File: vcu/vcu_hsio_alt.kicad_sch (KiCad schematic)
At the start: 51 parts, among them J5 FSUK_RTD, Q2 FDN359BN, Q3 FDN359BN, Q4 FDN359BN, Q5 FDN359BN, Q6 FDN359BN, Q7 FDN359BN, Q8 FDN359BN, U10 4504, U11 4504, U12 4504

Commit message: unbreaking git hopefully
pls work pls work pls work pls work pls work pls work pls work pls work pls work pls work pls work pls work pls work pls work pls work pls work pls work pls work pls work pls work pls work pls work pls work pls work
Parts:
- removed #SP1: KP1600, symbol Device:Speaker
- removed C49, C52: 1uF, Capacitor_SMD:C_0402_1005Metric, symbol Device:C_Small
- removed C50, C51: 0.1uF, Capacitor_SMD:C_0402_1005Metric, symbol Device:C_Small
- removed D14, D15, D16, D17, D18, D19, D20, D21: LED, LED_SMD:LED_0402_1005Metric, symbol Device:LED
- removed J5: FSUK_RTD, Connector_PinHeader_2.54mm:PinHeader_1x02_P2.54mm_Vertical, symbol Connector_Generic:Conn_02x01
- removed Q2, Q3, Q4, Q5, Q6, Q7, Q8: FDN359BN, Package_TO_SOT_SMD:SOT-23_Handsoldering, symbol SUFST:FDN359BN
- removed R62, R63, R64, R65, R66, R67, R68, R69: 1.5K, Resistor_SMD:R_0402_1005Metric, symbol Device:R_Small
- removed R70, R71, R72: 8.6K, Resistor_SMD:R_0402_1005Metric, symbol Device:R_Small
- removed R73, R74, R81, R82, R83, R84: 0, Resistor_SMD:R_0402_1005Metric, symbol Device:R_Small
- removed R75: 4.7K, Resistor_SMD:R_0402_1005Metric, symbol Device:R_Small
- removed R76: 1k, Resistor_SMD:R_0402_1005Metric, symbol Device:R_Small
- removed R77: 3k3, Resistor_SMD:R_0402_1005Metric, symbol Device:R_Small
- removed R78, R79, R80, R85, R86, R87: 1K, Resistor_SMD:R_0402_1005Metric, symbol Device:R_Small
- removed U10, U11, U12: 4504, Package_SO:SOIC-16W_5.3x10.2mm_P1.27mm, symbol 4xxx:4504
- removed U9: ~, Package_DFN_QFN:TQFN-32-1EP_5x5mm_P0.5mm_EP3.1x3.1mm_ThermalVias, symbol SUFST:MAX22195
- added #SP2: KP1600, symbol Device:Speaker
- added C64, C67: 1uF, Capacitor_SMD:C_0402_1005Metric, symbol Device:C_Small
- added C65, C66: 0.1uF, Capacitor_SMD:C_0402_1005Metric, symbol Device:C_Small
- added D22, D23, D24, D25, D26, D27, D28, D4: LED, LED_SMD:LED_0402_1005Metric, symbol Device:LED
- added J1: FSUK_RTD, Connector_PinHeader_2.54mm:PinHeader_1x02_P2.54mm_Vertical, symbol Connector_Generic:Conn_02x01
- added Q11, Q12, Q13, Q14, Q15, Q16, Q9: FDN359BN, Package_TO_SOT_SMD:SOT-23_Handsoldering, symbol SUFST:FDN359BN
- added R100, R101, R102, R103, R96, R97, R98, R99: 1.5K, Resistor_SMD:R_0402_1005Metric, symbol Device:R_Small
- added R104, R105, R106: 8.6K, Resistor_SMD:R_0402_1005Metric, symbol Device:R_Small
- added R107, R108, R115, R116, R117, R118: 0, Resistor_SMD:R_0402_1005Metric, symbol Device:R_Small
- added R109: 4.7K, Resistor_SMD:R_0402_1005Metric, symbol Device:R_Small
- added R110: 1k, Resistor_SMD:R_0402_1005Metric, symbol Device:R_Small
- added R111: 3k3, Resistor_SMD:R_0402_1005Metric, symbol Device:R_Small
- added R112, R113, R114, R119, R120, R121: 1K, Resistor_SMD:R_0402_1005Metric, symbol Device:R_Small
- added U15, U16, U22: 4504, Package_SO:SOIC-16W_5.3x10.2mm_P1.27mm, symbol 4xxx:4504
- added U6: ~, Package_DFN_QFN:TQFN-32-1EP_5x5mm_P0.5mm_EP3.1x3.1mm_ThermalVias, symbol SUFST:MAX22195
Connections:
- net +3V3: now also C66.2, C67.2, U15.16 (VDD), U16.1 (VCC), U22.1 (VCC), U6.28 (RDYEN), U6.31 (VDD3)
- net +5V: now also R108.2, R115.2, R116.2
- net +GLV_PROT: now also C64.2, C65.2, R104.1, R107.2, R117.2, R118.2, U6.30 (VDD24)
- net GND: now also C64.1, C65.1, C66.1, C67.1, D22.1 (K), D23.1 (K), D24.1 (K), D25.1 (K), D26.1 (K), D27.1 (K), D28.1 (K), D4.1 (K), Q11.2 (S), Q12.2 (S), Q13.2 (S), Q14.2 (S), Q15.2 (S), Q16.2 (S), Q9.2 (S), R105.2, R106.2, R109.1, R111.1, U15.8 (VSS), U16.8 (VSS), U22.8 (VSS), U6.25 (GND), U6.32 (GND), U6.EX (GND)
- net HSDI_GP1: now also R100.2
- net HSDI_GP10: now also U15.14 (Fin)
- net HSDI_GP2: now also R101.2
- net HSDI_GP3: now also R102.2
- net HSDI_GP4: now also R103.2
- net HSDI_GP5: now also U15.3 (Ain)
- net HSDI_GP6: now also U15.5 (Bin)
- net HSDI_GP7: now also U15.7 (Cin)
- net HSDI_GP8: now also U15.9 (Din)
- net HSDI_GP9: now also U15.11 (Ein)
- net HSDI_SCS1: now also R96.2
- net HSDI_SCS2: now also R97.2
- net HSDI_SCS3: now also R98.2
- net HSDI_SCS4: now also R99.2
- net HSDO_GP1: now also U16.12 (Eout)
- net HSDO_GP2: now also U16.15 (Fout)
- net HSDO_GP3: now also U22.2 (Aout)
- net HSDO_GP4: now also U22.4 (Bout)
- net HSDO_GP6: now also U22.6 (Cout)
- net HSDO_GP7: now also U22.10 (Dout)
- net HSDO_PWM1: now also U22.12 (Eout)
- net HSDO_PWM2: now also U22.15 (Fout)
- net HSDO_SCS1: now also U16.2 (Aout)
- net HSDO_SCS2: now also U16.4 (Bout)
- net HSDO_SCS3: now also U16.6 (Cout)
- net HSDO_SCS4: now also U16.10 (Dout)
- net LATCH_1: now also Q11.1 (G)
- net LATCH_2: now also Q12.1 (G)
- net LED_1: now also R112.2
- net LED_2: now also R113.2
- net LED_3: now also R114.2
- net LED_4: now also R119.2
- net LED_5: now also R120.2
- net LED_6: now also R121.2
- net LEVEL1_RDY: now also R109.2, U6.29 (READY)
- net LSDI_GP1: now also U6.13 (OP5)
- net LSDI_GP2: now also U6.14 (OP6)
- net LSDI_GP3: now also U6.15 (OP7), U6.16 (OP8)
- net LSDI_SCS1: now also U6.9 (OP1)
- net LSDI_SCS10: now also U15.15 (Fout)
- net LSDI_SCS2: now also U6.10 (OP2)
- net LSDI_SCS3: now also U6.11 (OP3)
- net LSDI_SCS4: now also U6.12 (OP4)
- net LSDI_SCS5: now also U15.2 (Aout)
- net LSDI_SCS6: now also U15.4 (Bout)
- net LSDI_SCS7: now also U15.6 (Cout)
- net LSDI_SCS8: now also U15.10 (Dout)
- net LSDI_SCS9: now also U15.12 (Eout)
- net LSDO_GP1: now also U16.11 (Ein)
- net LSDO_GP2: now also U16.14 (Fin)
- net LSDO_GP3: now also U22.3 (Ain)
- net LSDO_GP4: now also U22.5 (Bin)
- net LSDO_GP5: now also U22.7 (Cin)
- net LSDO_GP6: now also U22.9 (Din)
- net LSDO_PWM1: now also U22.11 (Ein)
- net LSDO_PWM2: now also U22.14 (Fin)
- net LSDO_SCS1: now also U16.3 (Ain)
- net LSDO_SCS2: now also U16.5 (Bin)
- net LSDO_SCS3: now also U16.7 (Cin)
- net LSDO_SCS4: now also U16.9 (Din)
- net LSD_LED_3: now also Q13.1 (G)
- net LSD_LED_4: now also Q14.1 (G)
- net LSD_LED_5: now also Q15.1 (G)
- net LSD_LED_6: now also Q16.1 (G)
- net LSD_R2D: now also Q9.1 (G), R111.2
- net R2DS-: now also J1.2 (Pin_2), R110.2
- new net: Q13.3 (D), R114.1
- new net: Q14.3 (D), R119.1
- new net: R107.1, R108.1, U15.1 (VCC)
- new net: Q15.3 (D), R120.1
- new net: J1.1 (Pin_1), Q9.3 (D), R110.1
- new net: R97.1, U6.3 (IN2)
- new net: R96.1, U6.1 (IN1)
- new net: D25.2 (A), U6.17 (LED5)
- new net: R100.1, U6.18 (IN5)
- new net: D26.2 (A), U6.19 (LED6)
- new net: D4.2 (A), U6.2 (LED1)
- new net: R101.1, U6.20 (IN6)
- new net: D27.2 (A), U6.21 (LED7)
- new net: R102.1, U6.22 (IN7)
- new net: D28.2 (A), U6.23 (LED8)
- new net: R103.1, U6.24 (IN8)
- new net: R106.1, U6.26 (REFDI)
- new net: R104.2, R105.1, U6.27 (EXTVM)
- new net: D22.2 (A), U6.4 (LED2)
- new net: R98.1, U6.5 (IN3)
- new net: D23.2 (A), U6.6 (LED3)
- new net: R99.1, U6.7 (IN4)
- new net: D24.2 (A), U6.8 (LED4)
- new net: R116.1, R118.1, U22.16 (VDD)
- new net: Q11.3 (D), R112.1
- new net: Q12.3 (D), R113.1
- new net: Q16.3 (D), R121.1
- new net: R115.1, R117.1, U16.16 (VDD)

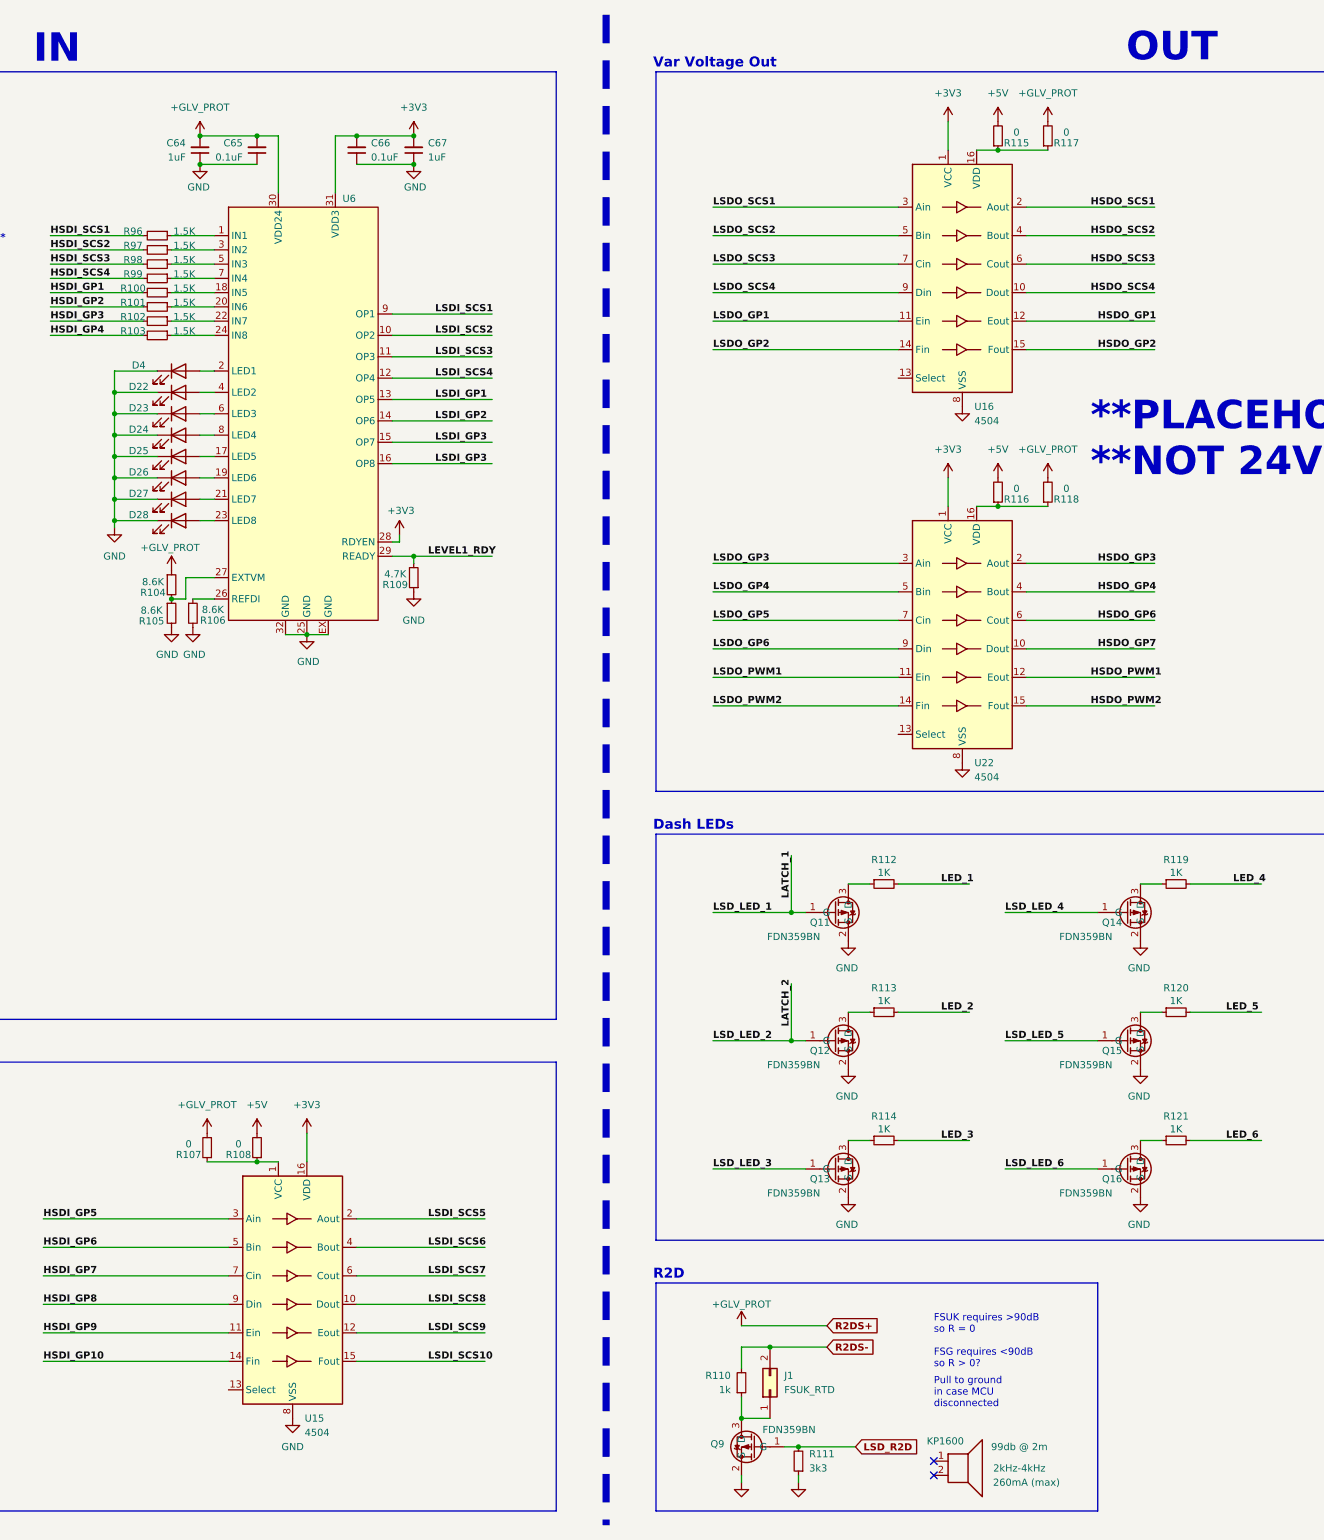
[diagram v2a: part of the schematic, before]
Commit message: Assigning MPNs for BOM
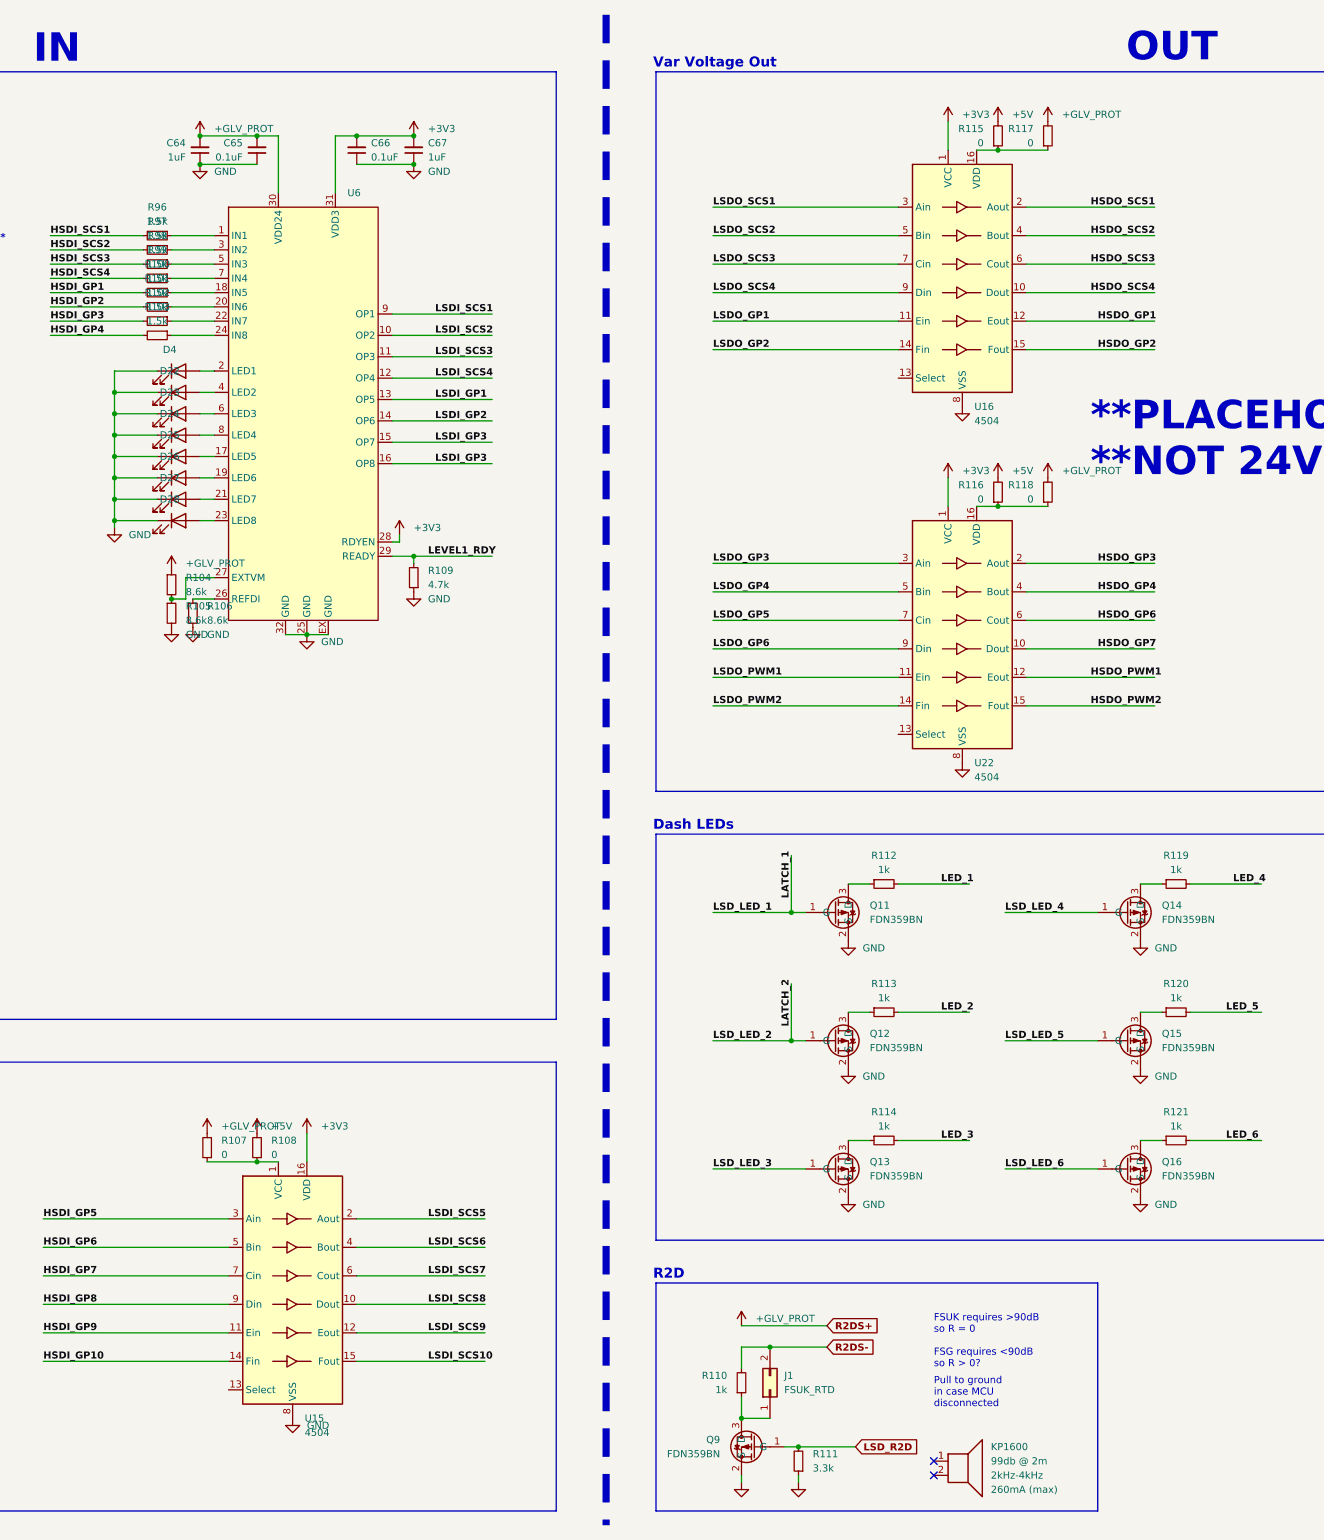
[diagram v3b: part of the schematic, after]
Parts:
- #SP2, C64, C65, C66, C67, D22, D23, D24, D25, D26, D27, D28, D4, J1, Q11, Q12, Q13, Q14, Q15, Q16, Q9, R107, R108, R110, R115, R116, R117, R118, U15, U16, U22, U6: now left out of the parts list
- R100, R101, R102, R103, R96, R97, R98, R99: value 1.5K -> 1.5k; now left out of the parts list
- R104, R105, R106: value 8.6K -> 8.6k; now left out of the parts list
- R109: value 4.7K -> 4.7k; now left out of the parts list
- R111: value 3k3 -> 3.3k; now left out of the parts list
- R112, R113, R114, R119, R120, R121: value 1K -> 1k; now left out of the parts list
